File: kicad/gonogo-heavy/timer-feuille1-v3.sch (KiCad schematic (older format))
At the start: 70 parts, among them J1 Screw_Terminal_01x02, J2 Screw_Terminal_01x04, K1 FINDER-30.22, Q1 2N2222, Q2 2N2222, SW1 SW_DIP_x08, SW2 SW_DIP_x04, SW3 SW_DIP_x08, SW4 SW_DIP_x04, U1 4011, U10 4071, U11 4012, U12 4012, U13 4011, U14 4071, U15 4040, U16 4068, U17 4071, U18 4071, U19 4012, U2 4071, U3 4040, U4 4060, U5 4068, U6 4071, U7 4013, U8 4011, U9 4040, Y1 32,768 kHz

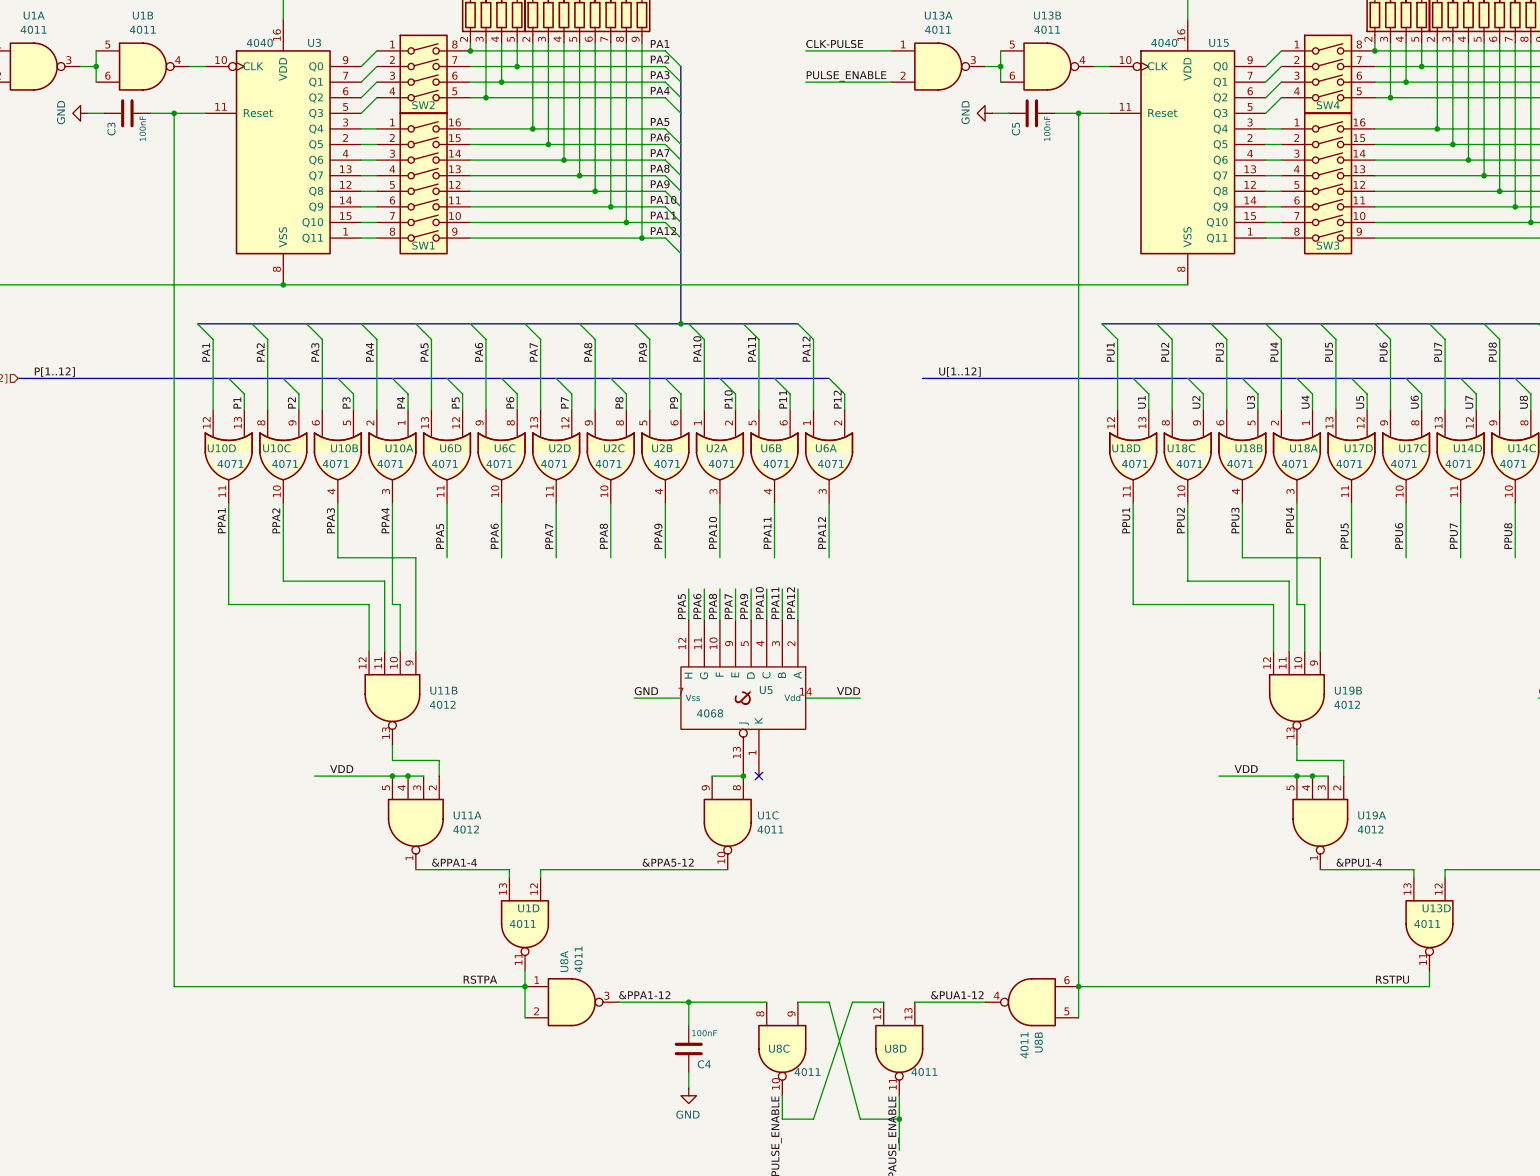
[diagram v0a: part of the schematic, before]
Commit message: Correction d'une erreur dans le schéma et le pcb
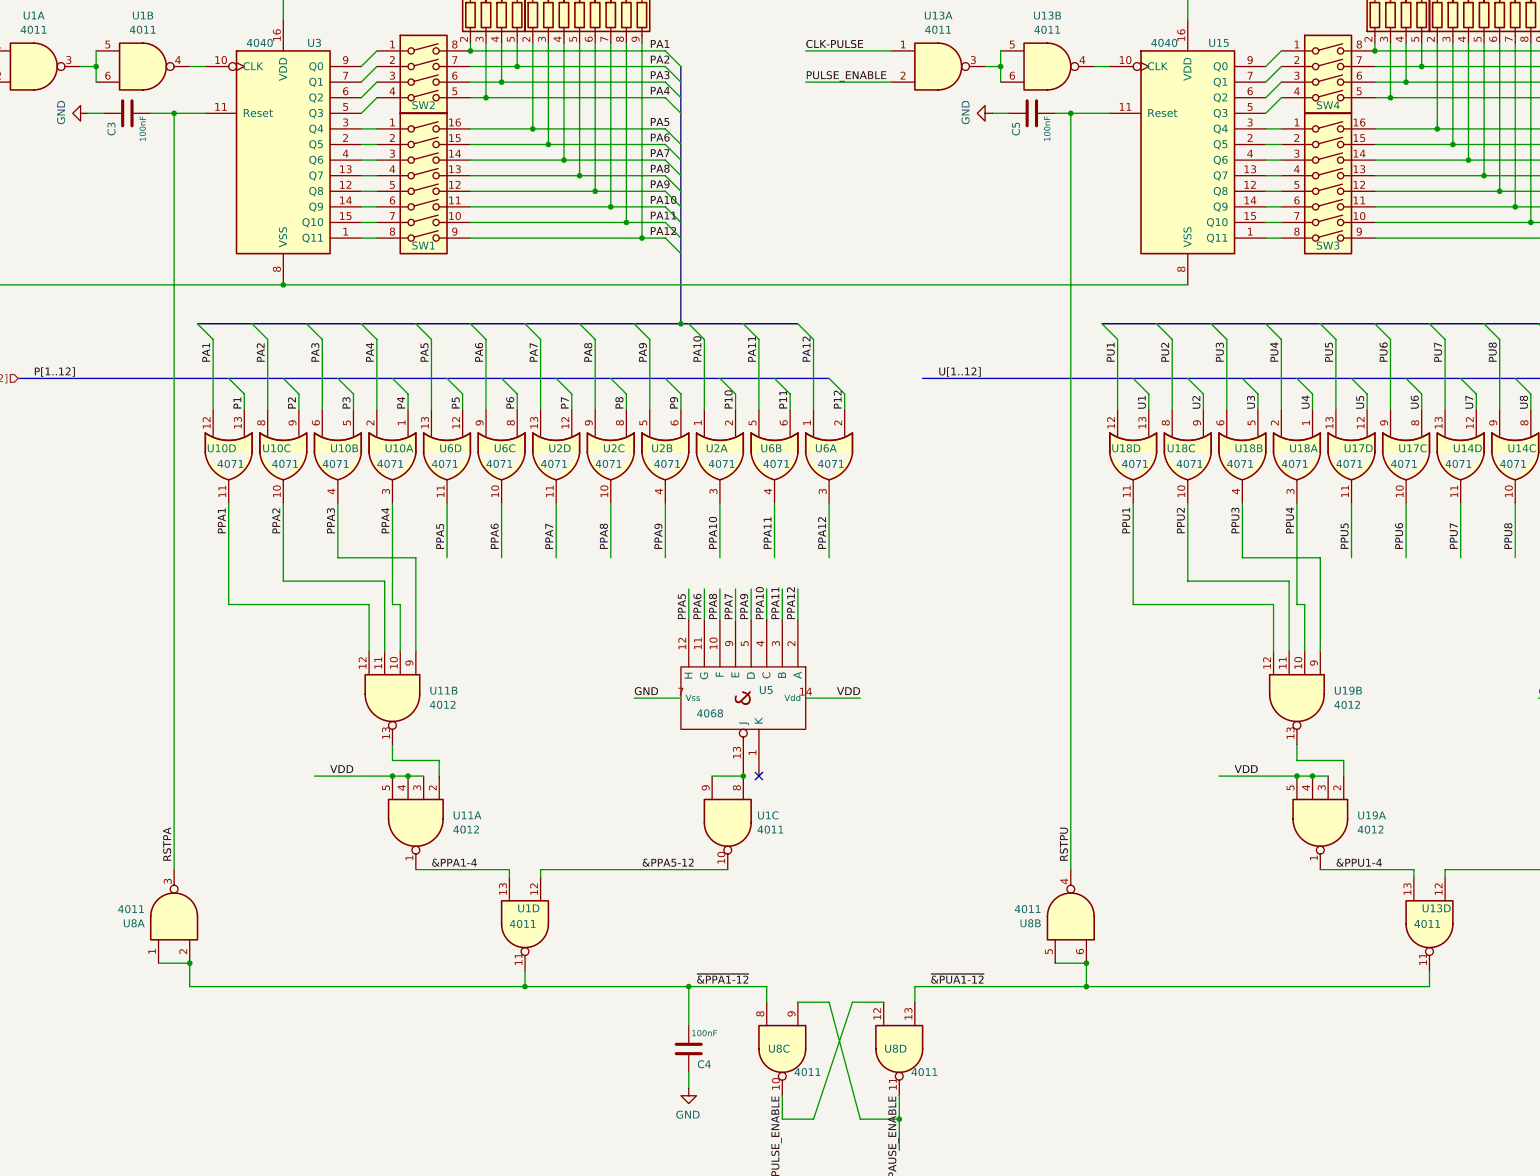
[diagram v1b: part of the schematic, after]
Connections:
- net labels added: ~&PPA1-12, ~&PUA1-12
- net labels removed: &PPA1-12, &PUA1-12
- wire segments 485 -> 489
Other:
- moved on the sheet: U8A, U8B
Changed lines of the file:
@@
 Sheet 3 3
 Title "GONOGO Heavy"
-Date "2021-01-29"
-Rev "3"
+Date "2021-02-10"
+Rev "4"
 Comp "D'JET Conseil"
 Comment1 "Conception : Jacques Ehrlich "
@@
 Wire Wire Line
 	4950 9550 4950 9650
-Wire Wire Line
-	4950 9650 2700 9650
-Wire Wire Line
-	2700 4050 2700 9650
 $Comp
 L 4xxx:4011 U1
@@
 	10750 9550 10750 9650
 Wire Wire Line
-	10750 9650 8500 9650
-Wire Wire Line
 	4600 3150 5000 3150
 Wire Wire Line
@@
 Wire Wire Line
 	5200 1300 5200 2200
-Wire Wire Line
-	6500 9750 6000 9750
-Wire Wire Line
-	6000 9900 6000 9750
-Connection ~ 6000 9750
 Wire Wire Line
 	6000 10200 6000 10300
@@
 L 4xxx:4011 U8
 U 1 1 600457D1
-P 5250 9750
-F 0 "U8" V 5204 9938 50  0000 L CNN
-F 1 "4011" V 5295 9938 50  0000 L CNN
-F 2 "Package_DIP:DIP-14_W7.62mm_Socket" H 5250 9750 50  0001 C CNN
-F 3 "http://www.intersil.com/content/dam/Intersil/documents/cd40/cd4011bms-12bms-23bms.pdf" H 5250 9750 50  0001 C CNN
-	1    5250 9750
-	1    0    0    -1
+P 2700 9200
+F 0 "U8" V 2654 9388 50  0000 L CNN
+F 1 "4011" V 2745 9388 50  0000 L CNN
+F 2 "Package_DIP:DIP-14_W7.62mm_Socket" H 2700 9200 50  0001 C CNN
+F 3 "http://www.intersil.com/content/dam/Intersil/documents/cd40/cd4011bms-12bms-23bms.pdf" H 2700 9200 50  0001 C CNN
+	1    2700 9200
+	0    -1   -1   0
 $EndComp
 Connection ~ 4950 9650
@@
 L 4xxx:4011 U8
 U 2 1 60083D9E
-P 8200 9750
-F 0 "U8" V 8154 9938 50  0000 L CNN
-F 1 "4011" V 8245 9938 50  0000 L CNN
-F 2 "Package_DIP:DIP-14_W7.62mm_Socket" H 8200 9750 50  0001 C CNN
-F 3 "http://www.intersil.com/content/dam/Intersil/documents/cd40/cd4011bms-12bms-23bms.pdf" H 8200 9750 50  0001 C CNN
-	2    8200 9750
-	-1   0    0    1
-$EndComp
-Connection ~ 8500 9650
-Wire Wire Line
-	7450 9750 7900 9750
-Wire Wire Line
-	5550 9750 6000 9750
-Wire Wire Line
-	4950 9850 4950 9650
-Wire Wire Line
-	8500 9850 8500 9650
+P 8450 9200
+F 0 "U8" V 8404 9388 50  0000 L CNN
+F 1 "4011" V 8495 9388 50  0000 L CNN
+F 2 "Package_DIP:DIP-14_W7.62mm_Socket" H 8450 9200 50  0001 C CNN
+F 3 "http://www.intersil.com/content/dam/Intersil/documents/cd40/cd4011bms-12bms-23bms.pdf" H 8450 9200 50  0001 C CNN
+	2    8450 9200
+	0    -1   -1   0
+$EndComp
 Wire Wire Line
 	5950 7800 5650 7800
@@
 	0    1    1    0
 $EndComp
-Wire Wire Line
-	8500 4050 8700 4050
 Wire Wire Line
 	9700 4150 9800 4150
@@
 Wire Wire Line
 	10850 8950 10850 8900
-Wire Wire Line
-	8500 4050 8500 9650
 $Comp
 L 4xxx:4011 U13
@@
 $EndComp
 Wire Wire Line
-	8350 4050 8500 4050
-Wire Wire Line
 	8050 4050 7950 4050
 $Comp
@@
 	0    1    -1   0
 $EndComp
-Connection ~ 8500 4050
 Wire Wire Line
 	11750 7800 11450 7800
@@
 Text Label 5700 8900 0    50   ~ 0
 &PPA5-12
-Text Label 5550 9750 0    50   ~ 0
-&PPA1-12
-Text Label 7550 9750 0    50   ~ 0
-&PUA1-12
+Text Label 6050 9650 0    50   ~ 0
+~&PPA1-12
+Text Label 7550 9650 0    50   ~ 0
+~&PUA1-12
 Text Label 10150 8900 0    50   ~ 0
 &PPU1-4
 Text Label 11500 8900 0    50   ~ 0
 &PPU5-12
-Text Label 4550 9650 0    50   ~ 0
+Text Label 2700 8850 1    50   ~ 0
 RSTPA
-Text Label 10400 9650 0    50   ~ 0
+Text Label 8450 8850 1    50   ~ 0
 RSTPU
 $Comp
@@
 	1    0    0    -1
 $EndComp
+Wire Wire Line
+	6500 9750 6500 9650
+Wire Wire Line
+	2700 4050 2700 8900
+Wire Wire Line
+	4950 9650 6000 9650
+Connection ~ 6000 9650
+Wire Wire Line
+	6000 9650 6000 9900
+Wire Wire Line
+	6000 9650 6500 9650
+Wire Wire Line
+	8350 4050 8450 4050
+Wire Wire Line
+	7450 9750 7450 9650
+Wire Wire Line
+	7450 9650 8550 9650
+Wire Wire Line
+	8450 4050 8450 8900
+Connection ~ 8450 4050
+Wire Wire Line
+	8450 4050 8700 4050
+Wire Wire Line
+	8350 9500 8550 9500
+Wire Wire Line
+	8550 9500 8550 9650
+Connection ~ 8550 9500
+Connection ~ 8550 9650
+Wire Wire Line
+	8550 9650 10750 9650
+Wire Wire Line
+	2600 9500 2800 9500
+Wire Wire Line
+	4950 9650 2800 9650
+Wire Wire Line
+	2800 9650 2800 9500
 Wire Bus Line
 	5950 5400 6700 5400
@@
 Wire Bus Line
 	7500 5750 13300 5750
+Connection ~ 2800 9500
 $EndSCHEMATC

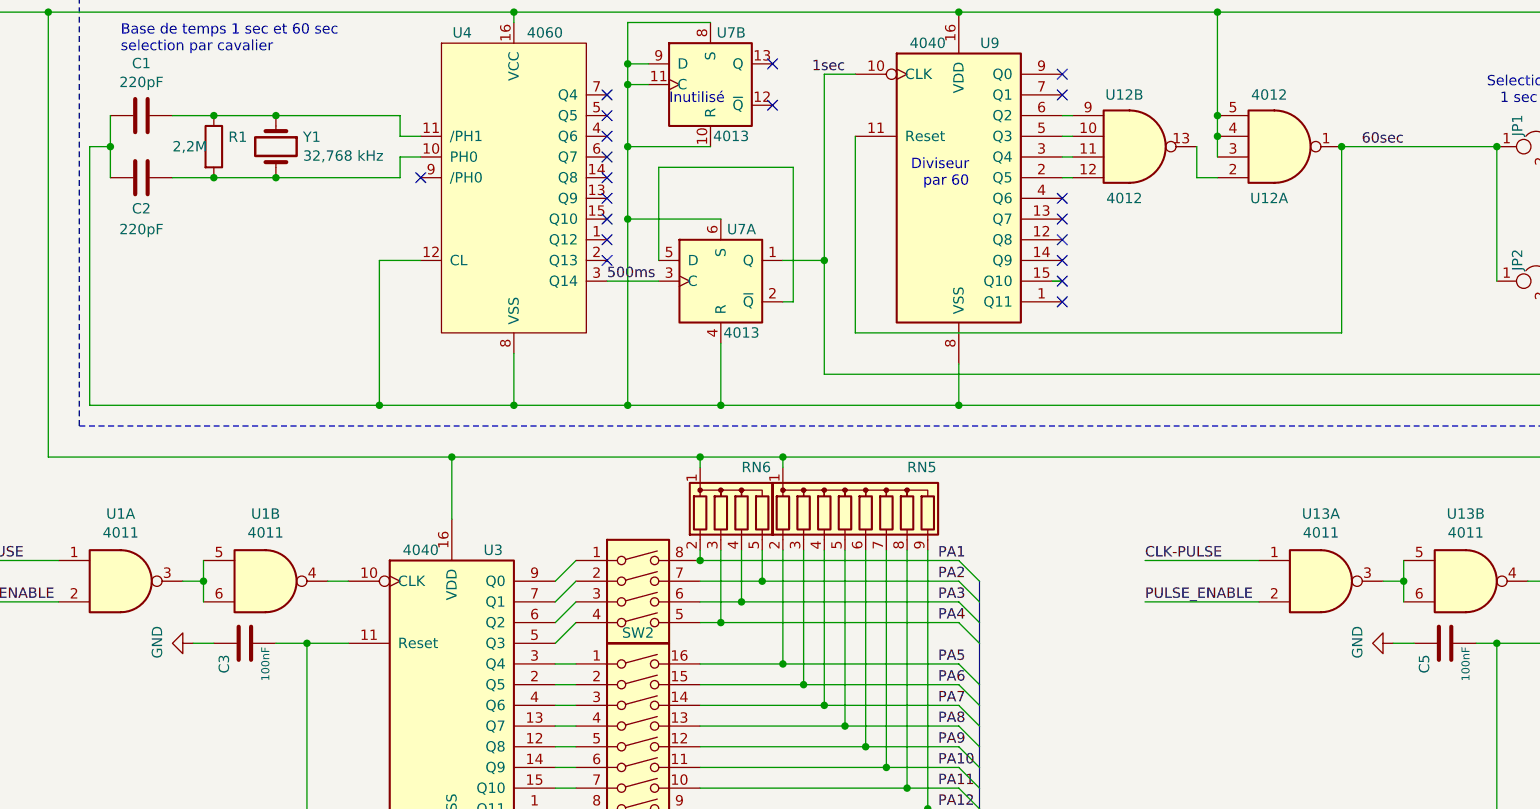
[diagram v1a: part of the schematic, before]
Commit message: correction des erreurs et ajout de capas de reset sur poweron
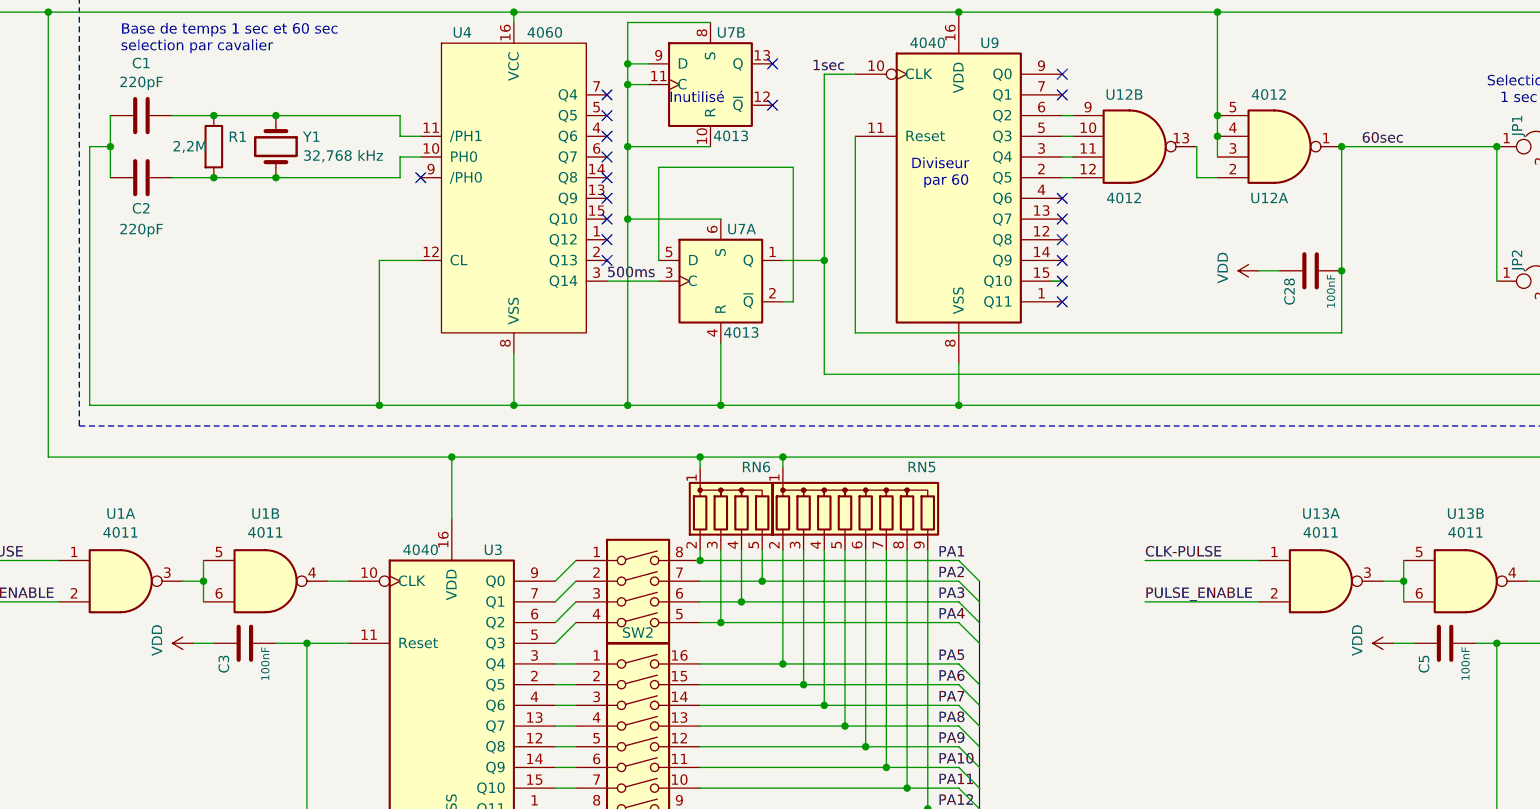
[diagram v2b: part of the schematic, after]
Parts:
- added C28: 100nF, Capacitor_THT:C_Rect_L7.2mm_W2.5mm_P5.00mm_FKS2_FKP2_MKS2_MKP2, symbol Device:C
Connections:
- wire segments 489 -> 491
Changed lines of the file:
@@
 Connection ~ 4700 2900
 Wire Wire Line
-	7700 1650 7700 2550
+	7700 1650 7700 2250
 Wire Wire Line
 	8700 2400 8700 2450
@@
 Wire Wire Line
 	2250 4050 2150 4050
-$Comp
-L power:GND #PWR01
-U 1 1 6040A5D1
-P 2150 4050
-F 0 "#PWR01" H 2150 3800 50  0001 C CNN
-F 1 "GND" H 2155 3877 50  0000 C CNN
-F 2 "" H 2150 4050 50  0001 C CNN
-F 3 "" H 2150 4050 50  0001 C CNN
-	1    2150 4050
-	0    1    -1   0
-$EndComp
 Connection ~ 2700 4050
 $Comp
@@
 Wire Wire Line
 	8050 4050 7950 4050
-$Comp
-L power:GND #PWR0101
-U 1 1 6023315D
-P 7950 4050
-F 0 "#PWR0101" H 7950 3800 50  0001 C CNN
-F 1 "GND" H 7955 3877 50  0000 C CNN
-F 2 "" H 7950 4050 50  0001 C CNN
-F 3 "" H 7950 4050 50  0001 C CNN
-	1    7950 4050
-	0    1    -1   0
-$EndComp
 Wire Wire Line
 	11750 7800 11450 7800
@@
 Wire Wire Line
 	2800 9650 2800 9500
+Connection ~ 2800 9500
+$Comp
+L Device:C C28
+U 1 1 603AED7C
+P 7550 2250
+F 0 "C28" H 7450 2350 50  0000 C CNN
+F 1 "100nF" H 7450 2150 39  0000 C CNN
+F 2 "Capacitor_THT:C_Rect_L7.2mm_W2.5mm_P5.00mm_FKS2_FKP2_MKS2_MKP2" H 7588 2100 50  0001 C CNN
+F 3 "~" H 7550 2250 50  0001 C CNN
+	1    7550 2250
+	0    -1   -1   0
+$EndComp
+Connection ~ 7700 2250
+Wire Wire Line
+	7700 2250 7700 2550
+$Comp
+L power:VDD #PWR0101
+U 1 1 603AFF4C
+P 7300 2250
+F 0 "#PWR0101" H 7300 2100 50  0001 C CNN
+F 1 "VDD" H 7315 2423 50  0000 C CNN
+F 2 "" H 7300 2250 50  0001 C CNN
+F 3 "" H 7300 2250 50  0001 C CNN
+	1    7300 2250
+	0    -1   -1   0
+$EndComp
+Wire Wire Line
+	7300 2250 7400 2250
 Wire Bus Line
 	5950 5400 6700 5400
@@
 Wire Bus Line
 	7500 5750 13300 5750
-Connection ~ 2800 9500
+$Comp
+L power:VDD #PWR0102
+U 1 1 603FAED1
+P 2150 4050
+F 0 "#PWR0102" H 2150 3900 50  0001 C CNN
+F 1 "VDD" H 2165 4223 50  0000 C CNN
+F 2 "" H 2150 4050 50  0001 C CNN
+F 3 "" H 2150 4050 50  0001 C CNN
+	1    2150 4050
+	0    -1   -1   0
+$EndComp
+$Comp
+L power:VDD #PWR0103
+U 1 1 603FCAC6
+P 7950 4050
+F 0 "#PWR0103" H 7950 3900 50  0001 C CNN
+F 1 "VDD" H 7965 4223 50  0000 C CNN
+F 2 "" H 7950 4050 50  0001 C CNN
+F 3 "" H 7950 4050 50  0001 C CNN
+	1    7950 4050
+	0    -1   -1   0
+$EndComp
 $EndSCHEMATC
